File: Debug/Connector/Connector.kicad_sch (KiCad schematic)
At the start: 9 parts, among them J1 AudioJack2_Ground, J2 AudioJack2_Ground, J3 Conn_Coaxial, J4 Conn_Coaxial, SW1 SW_SPDT

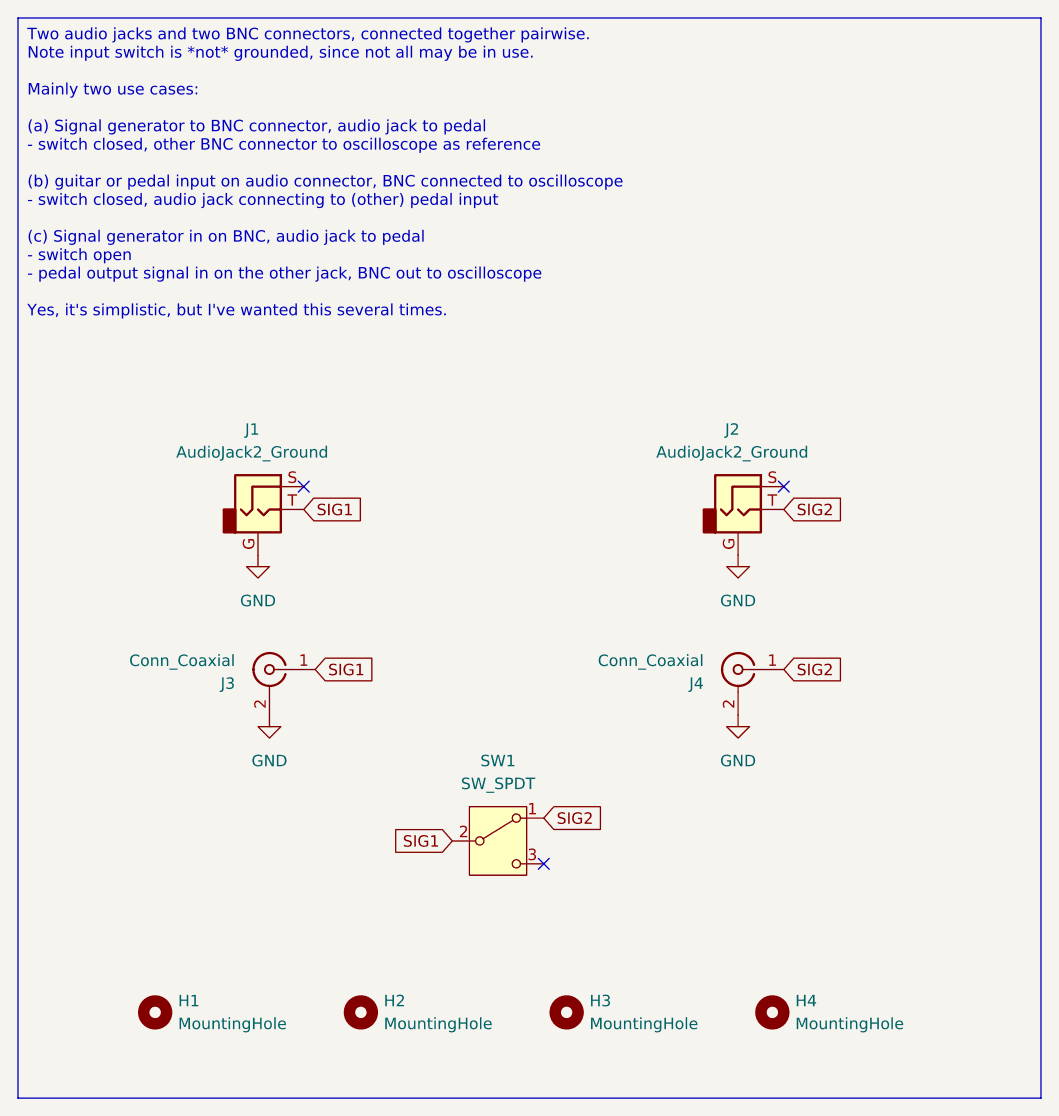
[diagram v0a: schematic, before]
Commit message: Commit some miscellaneous noise in the kicad files
This is partly just me updating the debug board to the kicad-9 file
format, and partly just re-annotating the tremolo board because of some
random movement changing the sorting order.

There should be no actual real changes in here.

Signed-off-by: Linus Torvalds <torvalds@linux-foundation.org>
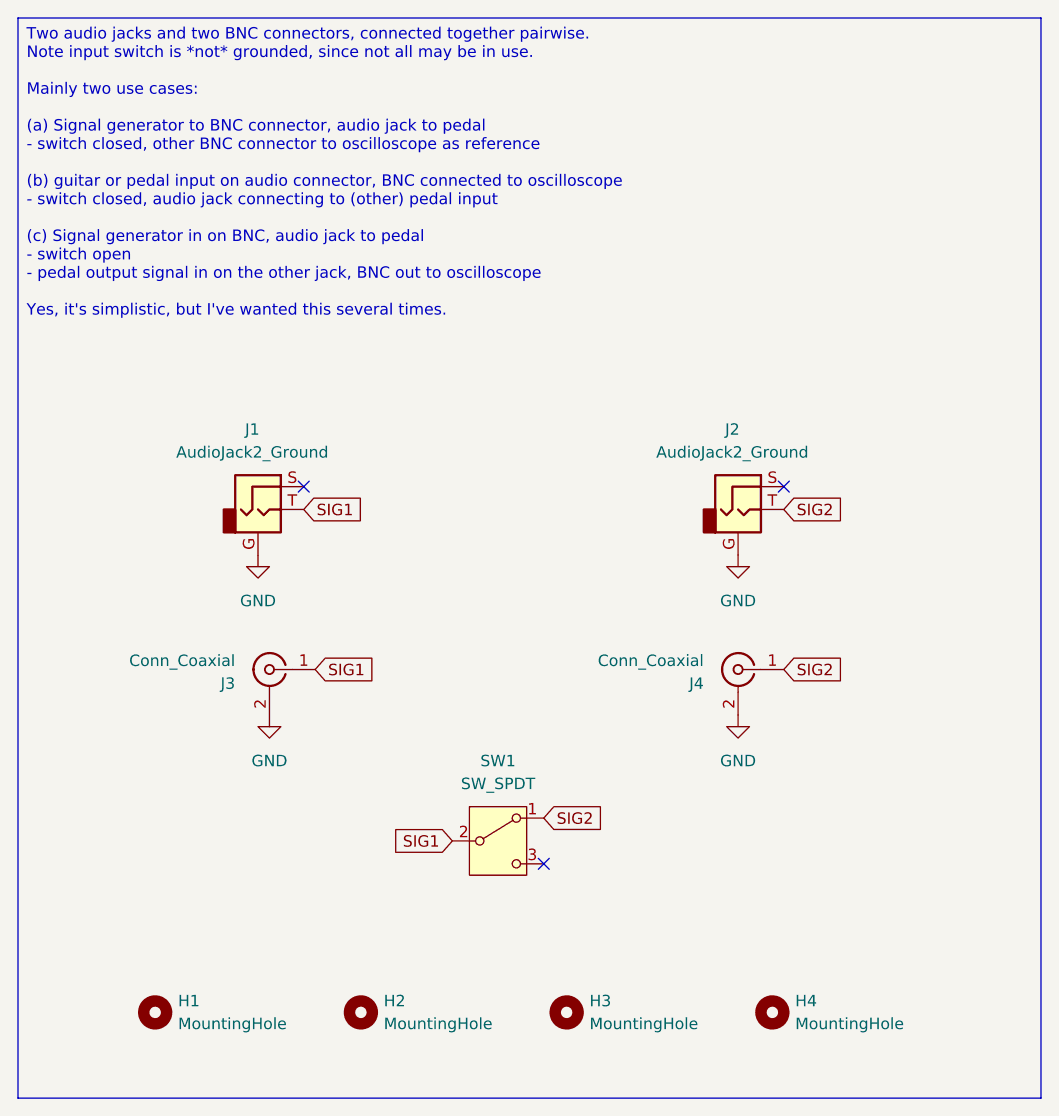
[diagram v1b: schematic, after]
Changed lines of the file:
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@@
 (kicad_sch
-	(version 20231120)
+	(version 20250114)
 	(generator "eeschema")
-	(generator_version "8.0")
+	(generator_version "9.0")
 	(paper "A4")
 	(title_block
@@
 		(rev "v1.0")
 	)
-	(no_connect
-		(at 72.39 107.95)
-	)
-	(no_connect
-		(at 99.06 66.04)
-	)
-	(no_connect
-		(at 45.72 66.04)
-	)
 	(text_box "Two audio jacks and two BNC connectors, connected together pairwise.\nNote input switch is *not* grounded, since not all may be in use.\n\nMainly two use cases:\n\n (a) Signal generator to BNC connector, audio jack to pedal\n      - switch closed, other BNC connector to oscilloscope as reference\n\n (b) guitar or pedal input on audio connector, BNC connected to oscilloscope\n       - switch closed, audio jack connecting to (other) pedal input\n\n (c) Signal generator in on BNC, audio jack to pedal\n       - switch open\n       - pedal output signal in on the other jack, BNC out to oscilloscope\n\nYes, it's simplistic, but I've wanted this several times."
 		(exclude_from_sim no)
 		(at 13.97 13.97 0)
 		(size 113.665 120.015)
+		(margins 0.9525 0.9525 0.9525 0.9525)
 		(stroke
 			(width 0)
@@
 			(justify left top)
 		)
+	)
+	(no_connect
+		(at 72.39 107.95)
+	)
+	(no_connect
+		(at 99.06 66.04)
+	)
+	(no_connect
+		(at 45.72 66.04)
 	)
 	(global_label "SIG2"
@@
 		(dnp no)
 		(fields_autoplaced yes)
-		(property "Reference" "#PWR1"
+		(property "Reference" "#PWR01"
 			(at 40.64 80.01 0)
 			(effects
@@
 			(project ""
 				(path "/9e337e0b-885b-4d2b-99a2-62cdd082c615"
-					(reference "#PWR1")
+					(reference "#PWR01")
 					(unit 1)
 				)
@@
 		(dnp no)
 		(fields_autoplaced yes)
-		(property "Reference" "#PWR4"
+		(property "Reference" "#PWR04"
 			(at 93.98 97.79 0)
 			(effects
@@
 			(project "Connector"
 				(path "/9e337e0b-885b-4d2b-99a2-62cdd082c615"
-					(reference "#PWR4")
+					(reference "#PWR04")
 					(unit 1)
 				)
@@
 		(dnp no)
 		(fields_autoplaced yes)
-		(property "Reference" "#PWR3"
+		(property "Reference" "#PWR03"
 			(at 41.91 97.79 0)
 			(effects
@@
 			(project "Connector"
 				(path "/9e337e0b-885b-4d2b-99a2-62cdd082c615"
-					(reference "#PWR3")
+					(reference "#PWR03")
 					(unit 1)
 				)
@@
 		(dnp no)
 		(fields_autoplaced yes)
-		(property "Reference" "#PWR2"
+		(property "Reference" "#PWR02"
 			(at 93.98 80.01 0)
 			(effects
@@
 			(project ""
 				(path "/9e337e0b-885b-4d2b-99a2-62cdd082c615"
-					(reference "#PWR2")
+					(reference "#PWR02")
 					(unit 1)
 				)
@@
 		)
 	)
+	(embedded_fonts no)
 )
